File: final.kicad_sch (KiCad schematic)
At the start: 27 parts, among them J1 Conn_02x16_Odd_Even, J2 USB_C_Receptacle_PowerOnly_6P, SW1 SW_Push, U2 INA219AxD, U3 BQ25601, U4 CH224K

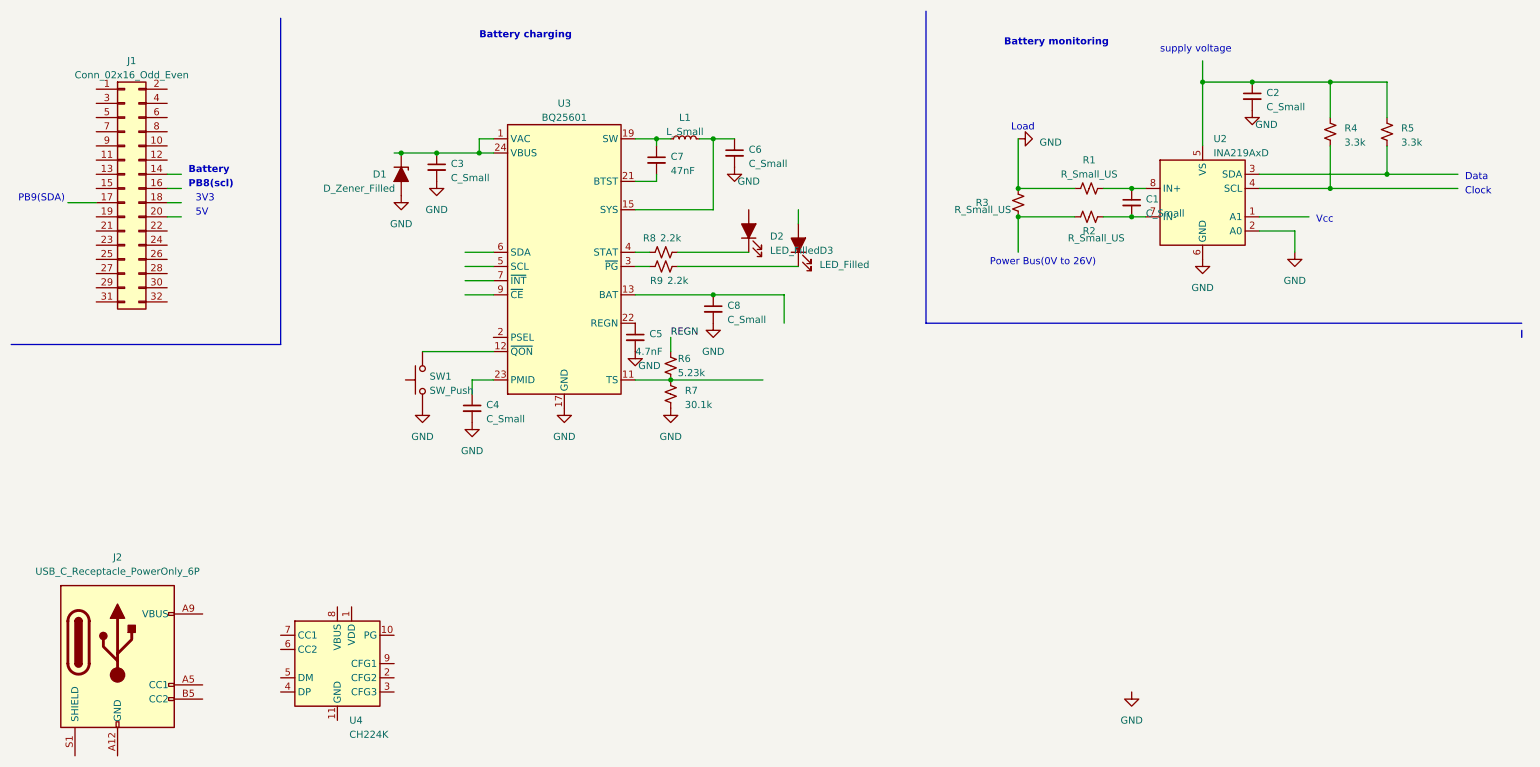
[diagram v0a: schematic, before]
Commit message: resolving electric checklist issues
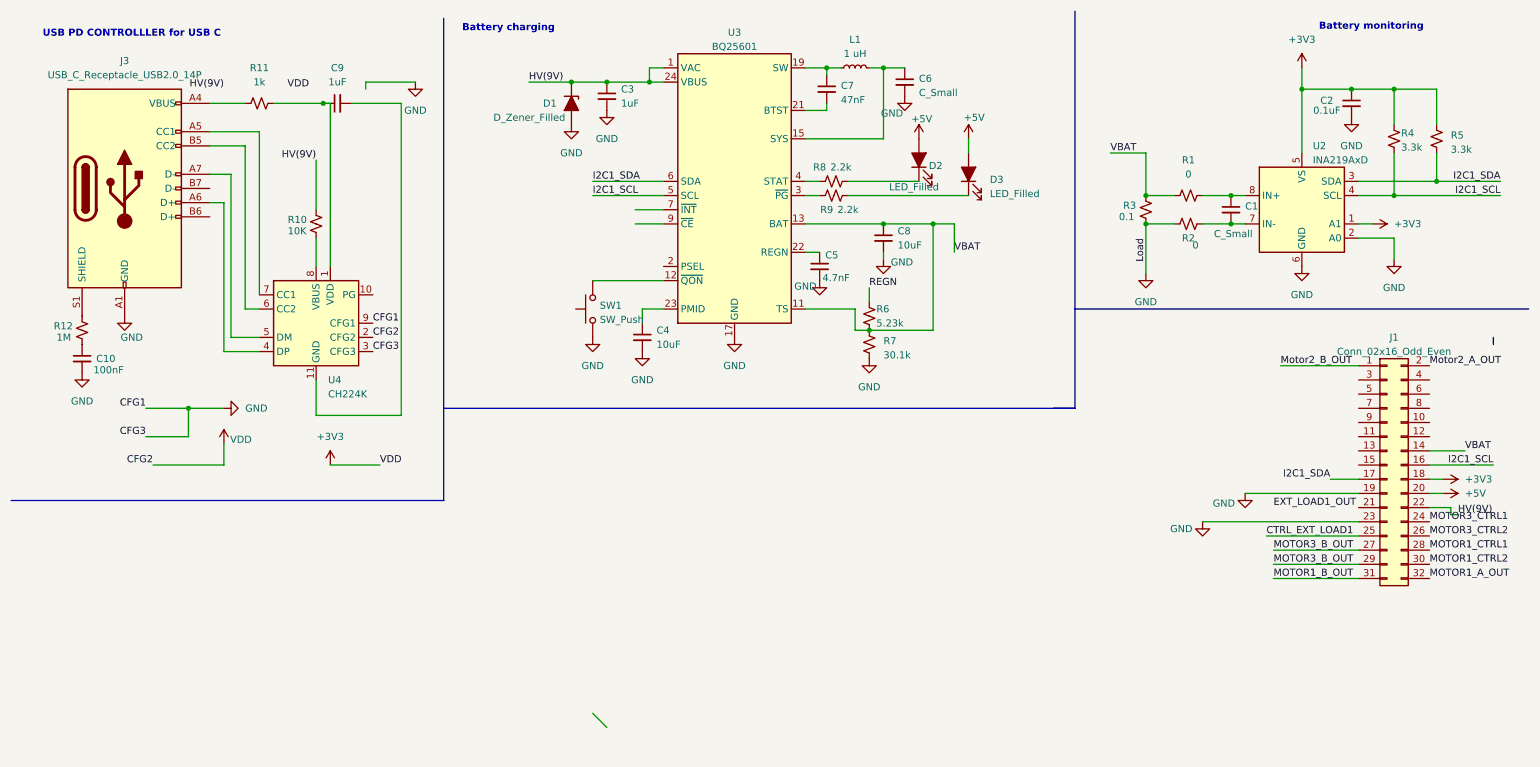
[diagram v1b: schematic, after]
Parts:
- removed J2: USB_C_Receptacle_PowerOnly_6P, symbol Connector:USB_C_Receptacle_PowerOnly_6P
- added C10: 100nF, symbol Device:C_Small
- added C9: 1uF, symbol Device:C_Small
- added J3: USB_C_Receptacle_USB2.0_14P, symbol Connector:USB_C_Receptacle_USB2.0_14P
- added R10: 10K, symbol Device:R_Small_US
- added R11: 1k, symbol Device:R_Small_US
- added R12: 1M, symbol Device:R_Small_US
- C2: value C_Small -> 0.1uF
- C3: value C_Small -> 1uF
- C4, C8: value C_Small -> 10uF
- L1: value L_Small -> 1 uH
- R1, R2: value R_Small_US -> 0
- R3: value R_Small_US -> 0.1
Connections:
- net GND: now also J1.19 (Pin_19), J1.23 (Pin_23), R2.1, R3.2, U4.3 (CFG3), U4.9 (CFG1), C10.2, J3.A1 (GND), J3.A12 (GND), J3.B1 (GND), J3.B12 (GND); no longer R1.1, R3.1
- net VBAT: now reaches C8.1, U3.13 (BAT), U3.14 (BAT)
- net VBAT: now also J1.14 (Pin_14), R1.1, R3.1, R6.2, R7.1, U3.11 (TS)
- net HV(9V): now reaches C3.1, D1.1 (K), U3.1 (VAC), U3.24 (VBUS)
- net HV(9V): now also J1.22 (Pin_22), R10.1
- net I2C1_SCL: now reaches U3.5 (SCL)
- net I2C1_SCL: now also J1.16 (Pin_16), R4.2, U2.4 (SCL)
- net I2C1_SDA: now reaches U3.6 (SDA)
- net I2C1_SDA: now also J1.17 (Pin_17), R5.2, U2.3 (SDA)
- net at U4.1 (VDD): now also C9.1, R11.2
- net at U4.11 (GND): now also C9.2
- net +3V3: now reaches U4.2 (CFG2)
- net +3V3: now also C2.1, J1.18 (Pin_18), R4.1, R5.1, U2.1 (A1), U2.5 (VS)
- net at U4.4 (DP): now also J3.A6 (D+)
- net at U4.5 (DM): now also J3.A7 (D-)
- net at U4.6 (CC2): now also J3.B5 (CC2)
- net at U4.7 (CC1): now also J3.A5 (CC1)
- net at U4.8 (VBUS): now also R10.2
- net +5V: now reaches D3.2 (A)
- net +5V: now also D2.2 (A), J1.20 (Pin_20)
- net Motor2_B_OUT: now reaches J1.1 (Pin_1)
- net Motor2_A_OUT: now reaches J1.2 (Pin_2)
- net MOTOR3_CTRL1: now reaches J1.24 (Pin_24)
- net CTRL_EXT_LOAD1: now reaches J1.25 (Pin_25)
- net MOTOR3_CTRL2: now reaches J1.26 (Pin_26)
- net MOTOR3_B_OUT: now reaches J1.27 (Pin_27)
- net MOTOR3_B_OUT: now also J1.29 (Pin_29)
- net MOTOR1_CTRL1: now reaches J1.28 (Pin_28)
- net MOTOR1_CTRL2: now reaches J1.30 (Pin_30)
- net MOTOR1_B_OUT: now reaches J1.31 (Pin_31)
- net MOTOR1_A_OUT: now reaches J1.32 (Pin_32)
- new net: J3.A4 (VBUS), J3.A9 (VBUS), J3.B4 (VBUS), J3.B9 (VBUS), R11.1
- new net: J3.S1 (SHIELD), R12.1
- new net: C10.1, R12.2
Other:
- note added: "USB PD CONTROLLLER for USB C"
- note removed: "3V3"
- note removed: "5V"
- note removed: "Battery"
- note removed: "Clock"
- note removed: "Data"
- note removed: "Load"
- note removed: "PB8(scl)"
- note removed: "PB9(SDA)"
- note removed: "Power Bus(0V to 26V)"
- note removed: "Vcc"
- note removed: "supply voltage"
- moved on the sheet: C1, C2, C3, C4, C5, C6, C7, C8, D1, D2, D3, J1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
